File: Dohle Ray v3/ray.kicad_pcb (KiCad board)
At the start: 2 copper layers, 50 x 91.6 mm, 33 parts, among them J1 Conn_01x07_Female, J2 AudioJack3, J3 AudioJack3, Q1 J201, SW1 3pdt_footswitch, U1 TL082

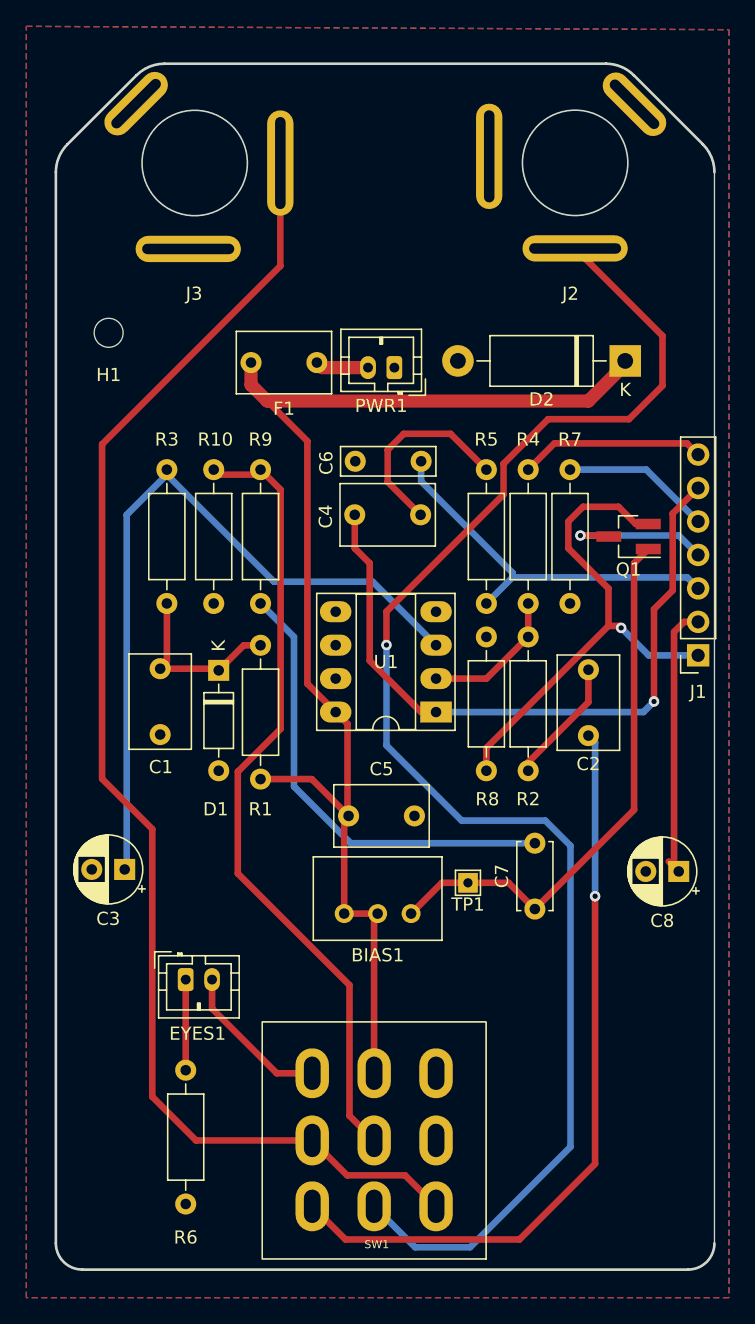
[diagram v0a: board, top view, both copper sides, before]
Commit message: Update version and fix faulty jack wiring
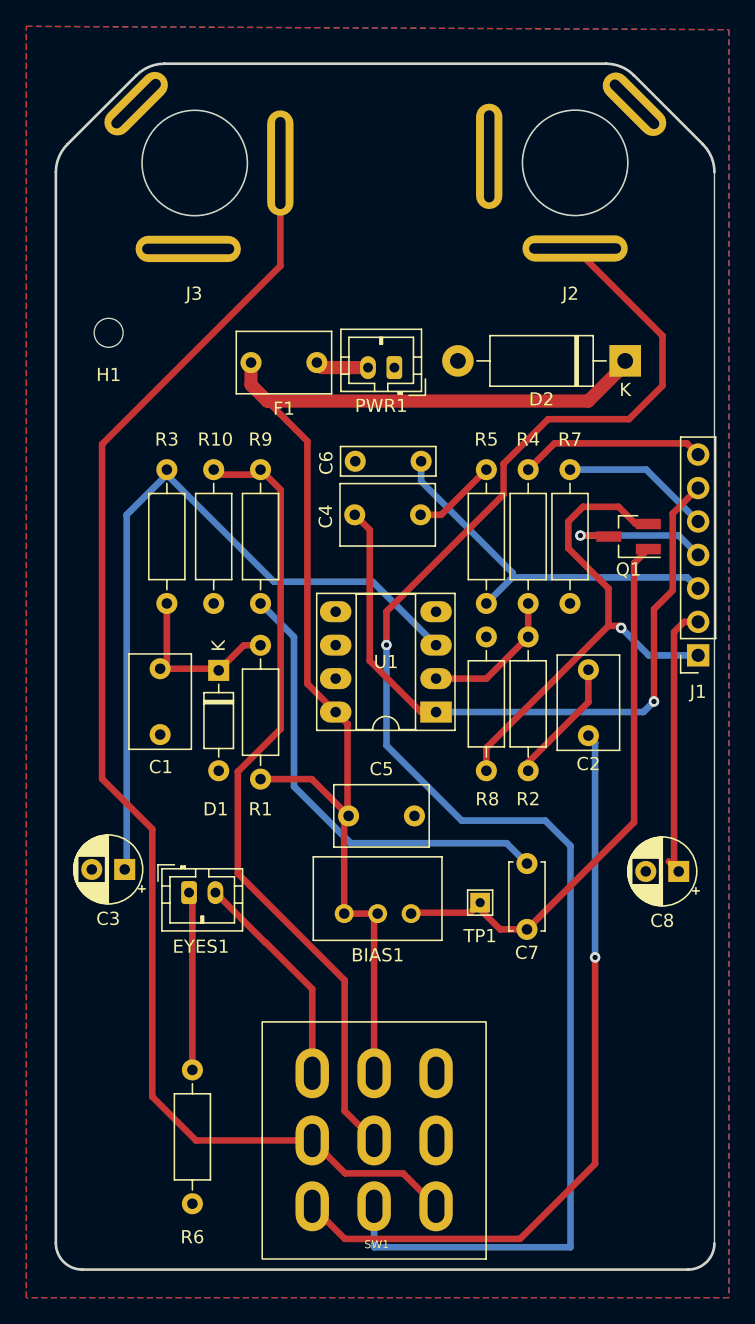
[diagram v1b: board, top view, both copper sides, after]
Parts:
- moved EYES1 6.61 mm to (105.7, 124.2)
- moved TP1 1.77 mm to (127.8, 125.0)
- moved C7 1.66 mm to (131.3, 127.0)
- moved R6 0.51 mm to (105.9, 137.7)
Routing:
- net Net-(C4-Pad2): track 15.1 -> 6.41 mm
- net Net-(EYES1-Pad1): track 6.88 -> 13.6 mm
- net Net-(J2-PadT): track 112.1 -> 118.4 mm
- net Net-(EYES1-Pad2): track 11.8 -> 16.8 mm
- net Net-(BIAS1-Pad3): track 42.1 -> 43.0 mm
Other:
- board text added: "Dohle Ray v3.1a"
- board text added: "Published under CC BY-NC-SA 3.0 license"
- board text removed: "Dohle Ray v3.0a"

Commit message: Update resistor values to have unity gain at 0% volume and gain knob, update PCB revision
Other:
- board text added: "Dohle Ray v3.1"
- board text removed: "Dohle Ray v3.1a"
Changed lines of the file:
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@@
       (xy 103.147567 144.703117)
     ) (layer "B.SilkS") (width 0.034835) (fill solid))
-  (gr_line (start 109.833016 132.77358) (end 109.833016 131.75758) (layer "B.Mask") (width 0.25))
-  (gr_line (start 110.348594 132.265214) (end 109.332594 132.265214) (layer "B.Mask") (width 0.25))
-  (gr_rect (start 110.819121 133.270739) (end 108.863321 131.289539) (layer "B.Mask") (width 0.25) (fill none))
+  (gr_line (start 109.068683 132.77358) (end 109.068683 131.75758) (layer "B.Mask") (width 0.25))
+  (gr_line (start 109.584261 132.265214) (end 108.568261 132.265214) (layer "B.Mask") (width 0.25))
+  (gr_rect (start 110.054788 133.270739) (end 108.098988 131.289539) (layer "B.Mask") (width 0.25) (fill none))
   (gr_line (start 113.152141 134.009276) (end 113.152141 133.509276) (layer "Dwgs.User") (width 0.2))
   (gr_line (start 124.052141 152.009276) (end 126.252141 152.009276) (layer "Dwgs.User") (width 0.2))
@@
     (effects (font (size 1.5 1.5) (thickness 0.2)) (justify mirror))
   )
-  (gr_text "Made in Switzerland" (at 121.668333 132.255387) (layer "B.Mask")
+  (gr_text "Made in Switzerland" (at 120.904 132.255387) (layer "B.Mask")
     (effects (font (size 1.3 1.3) (thickness 0.25)) (justify mirror))
   )
-  (gr_text "Dohle Ray v3.1a\n" (at 119.4212 129.3568) (layer "B.Mask")
+  (gr_text "Dohle Ray v3.1" (at 119.4212 129.3568) (layer "B.Mask")
     (effects (font (size 1.3 1.3) (thickness 0.25)) (justify mirror))
   )
